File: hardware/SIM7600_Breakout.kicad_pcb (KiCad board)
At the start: 4 copper layers, 40 x 80 mm, 68 parts, among them J1 SIM8060-6-0-14-00-A, J2 2W Header, J3 MJ-3502N, J4 30W Header, J5 2137160001, J6 U.FL-R-SMT-1(01), J7 U.FL-R-SMT-1(01), J8 U.FL-R-SMT-1(01), Q1 MMBT3904L_RFG, U1 NVT2008PW_118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

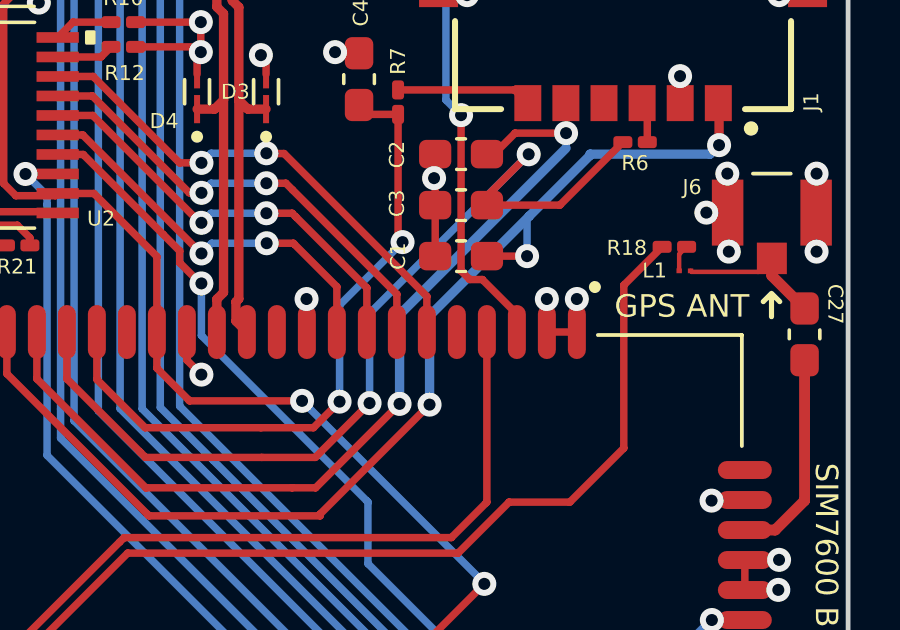
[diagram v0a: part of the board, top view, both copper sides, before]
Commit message: Updated README & added KiCad image generator action
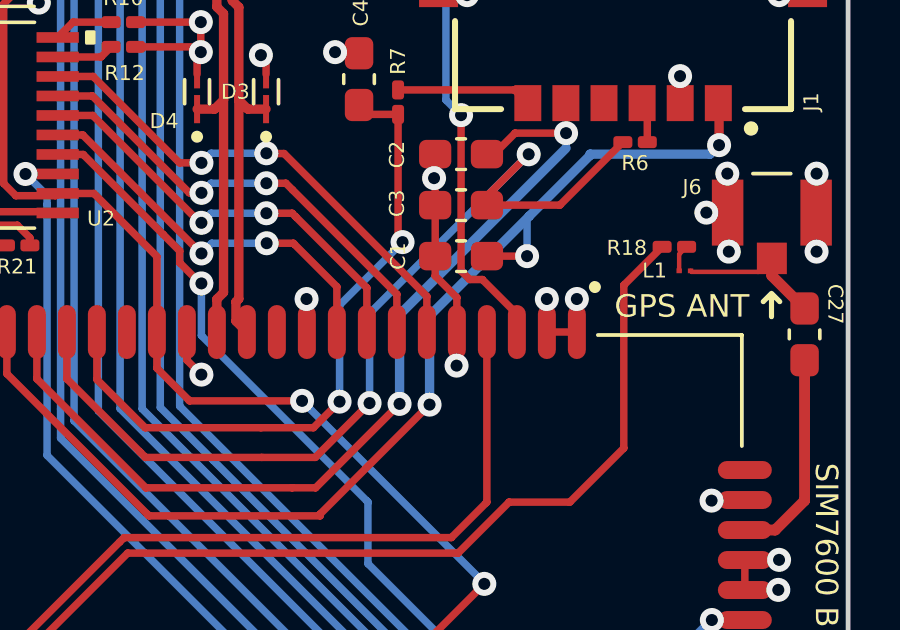
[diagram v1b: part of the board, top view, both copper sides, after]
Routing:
- net GND: track 104.9 -> 108.8 mm, vias 83 -> 84
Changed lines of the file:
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@@
 		)
 		(property "Value" "5K1"
-			(at 0 1.05 360)
+			(at 0 1.05 0)
 			(layer "F.Fab")
 			(effects
@@
 		)
 		(property "Footprint" ""
-			(at 0 0 360)
+			(at 0 0 0)
 			(layer "F.Fab")
 			(hide yes)
@@
 		)
 		(property "Datasheet" ""
-			(at 0 0 360)
+			(at 0 0 0)
 			(layer "F.Fab")
 			(hide yes)
@@
 		)
 		(property "Description" "Resistor, small US symbol"
-			(at 0 0 360)
+			(at 0 0 0)
 			(layer "F.Fab")
 			(hide yes)
@@
 		)
 		(fp_text user "${REFERENCE}"
-			(at 0 -0.68 360)
+			(at 0 -0.68 0)
 			(layer "F.Fab")
 			(effects
@@
 		)
 		(property "Value" "22"
-			(at 0 1.05 360)
+			(at 0 1.05 0)
 			(layer "F.Fab")
 			(effects
@@
 		)
 		(property "Footprint" ""
-			(at 0 0 360)
+			(at 0 0 0)
 			(layer "F.Fab")
 			(hide yes)
@@
 		)
 		(property "Datasheet" ""
-			(at 0 0 360)
+			(at 0 0 0)
 			(layer "F.Fab")
 			(hide yes)
@@
 		)
 		(property "Description" "Resistor, small US symbol"
-			(at 0 0 360)
+			(at 0 0 0)
 			(layer "F.Fab")
 			(hide yes)
@@
 		)
 		(fp_text user "${REFERENCE}"
-			(at 0 -0.68 360)
+			(at 0 -0.68 0)
 			(layer "F.Fab")
 			(effects
@@
 		(tags "resistor handsolder")
 		(property "Reference" "R5"
-			(at -1.283 0 360)
+			(at -1.283 0 0)
 			(layer "F.SilkS")
 			(effects
@@
 		)
 		(property "Value" "22pF"
-			(at 0 1.43 360)
+			(at 0 1.43 0)
 			(layer "F.Fab")
 			(effects
@@
 		)
 		(property "Footprint" ""
-			(at 0 0 360)
+			(at 0 0 0)
 			(layer "F.Fab")
 			(hide yes)
@@
 		)
 		(property "Datasheet" ""
-			(at 0 0 360)
+			(at 0 0 0)
 			(layer "F.Fab")
 			(hide yes)
@@
 		)
 		(property "Description" "Unpolarized capacitor, small symbol"
-			(at 0 0 360)
+			(at 0 0 0)
 			(layer "F.Fab")
 			(hide yes)
@@
 		)
 		(fp_text user "${REFERENCE}"
-			(at 0 0 360)
+			(at 0 0 0)
 			(layer "F.Fab")
 			(effects
@@
 		)
 		(property "Value" "47k"
-			(at 0 1.05 360)
+			(at 0 1.05 0)
 			(layer "F.Fab")
 			(effects
@@
 		)
 		(property "Footprint" ""
-			(at 0 0 360)
+			(at 0 0 0)
 			(layer "F.Fab")
 			(hide yes)
@@
 		)
 		(property "Datasheet" ""
-			(at 0 0 360)
+			(at 0 0 0)
 			(layer "F.Fab")
 			(hide yes)
@@
 		)
 		(property "Description" "Resistor, small US symbol"
-			(at 0 0 360)
+			(at 0 0 0)
 			(layer "F.Fab")
 			(hide yes)
@@
 		)
 		(fp_text user "${REFERENCE}"
-			(at 0 -0.68 360)
+			(at 0 -0.68 0)
 			(layer "F.Fab")
 			(effects
@@
 		)
 		(property "Value" "4k7"
-			(at 0 1.05 360)
+			(at 0 1.05 0)
 			(layer "F.Fab")
 			(effects
@@
 		)
 		(property "Footprint" ""
-			(at 0 0 360)
+			(at 0 0 0)
 			(layer "F.Fab")
 			(hide yes)
@@
 		)
 		(property "Datasheet" ""
-			(at 0 0 360)
+			(at 0 0 0)
 			(layer "F.Fab")
 			(hide yes)
@@
 		)
 		(property "Description" "Resistor, small US symbol"
-			(at 0 0 360)
+			(at 0 0 0)
 			(layer "F.Fab")
 			(hide yes)
@@
 		)
 		(fp_text user "${REFERENCE}"
-			(at 0 -0.68 360)
+			(at 0 -0.68 0)
 			(layer "F.Fab")
 			(effects
@@
 		)
 		(property "Value" "SIM8060-6-0-14-00-A"
-			(at 8.911805 8.071155 360)
+			(at 8.911805 8.071155 0)
 			(layer "F.Fab")
 			(effects
@@
 		)
 		(property "Footprint" ""
-			(at 0 0 360)
+			(at 0 0 0)
 			(layer "F.Fab")
 			(hide yes)
@@
 		)
 		(property "Datasheet" ""
-			(at 0 0 360)
+			(at 0 0 0)
 			(layer "F.Fab")
 			(hide yes)
@@
 		)
 		(property "Description" ""
-			(at 0 0 360)
+			(at 0 0 0)
 			(layer "F.Fab")
 			(hide yes)
@@
 	)
 	(segment
+		(start 145.96 88.78)
+		(end 145.2375 88.0575)
+		(width 0.25)
+		(layer "F.Cu")
+		(net 2)
+	)
+	(segment
 		(start 154.985 87.21)
 		(end 155.025 87.25)
@@
 	)
 	(segment
+		(start 145.96 91.04)
+		(end 145.95 91.05)
+		(width 0.25)
+		(layer "F.Cu")
+		(net 2)
+	)
+	(segment
 		(start 144.6525 124.96)
 		(end 144.6525 123.6625)
@@
 	)
 	(segment
+		(start 145.2375 88.0575)
+		(end 145.2375 87.4)
+		(width 0.25)
+		(layer "F.Cu")
+		(net 2)
+	)
+	(segment
 		(start 137.425 79.6)
 		(end 137.425 80.6)
@@
 	)
 	(segment
+		(start 145.96 89.93)
+		(end 145.96 91.04)
+		(width 0.25)
+		(layer "F.Cu")
+		(net 2)
+	)
+	(segment
 		(start 156.67 98.53)
 		(end 156.675 98.525)
@@
 	)
 	(segment
+		(start 145.96 89.93)
+		(end 145.96 88.78)
+		(width 0.25)
+		(layer "F.Cu")
+		(net 2)
+	)
+	(segment
 		(start 141.9375 80.6375)
 		(end 141.9 80.6)
@@
 		(size 0.8)
 		(drill 0.4)
+		(layers "F.Cu" "B.Cu")
+		(net 2)
+	)
+	(via
+		(at 145.95 91.05)
+		(size 0.8)
+		(drill 0.4)
